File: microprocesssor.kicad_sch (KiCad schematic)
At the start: 8 parts, among them U1 MC68B09, U11 74LS138, U2 MC68B40, U4 27128, U5 HM62256BLP, U6 74LS139, X1 CXO_DIP8

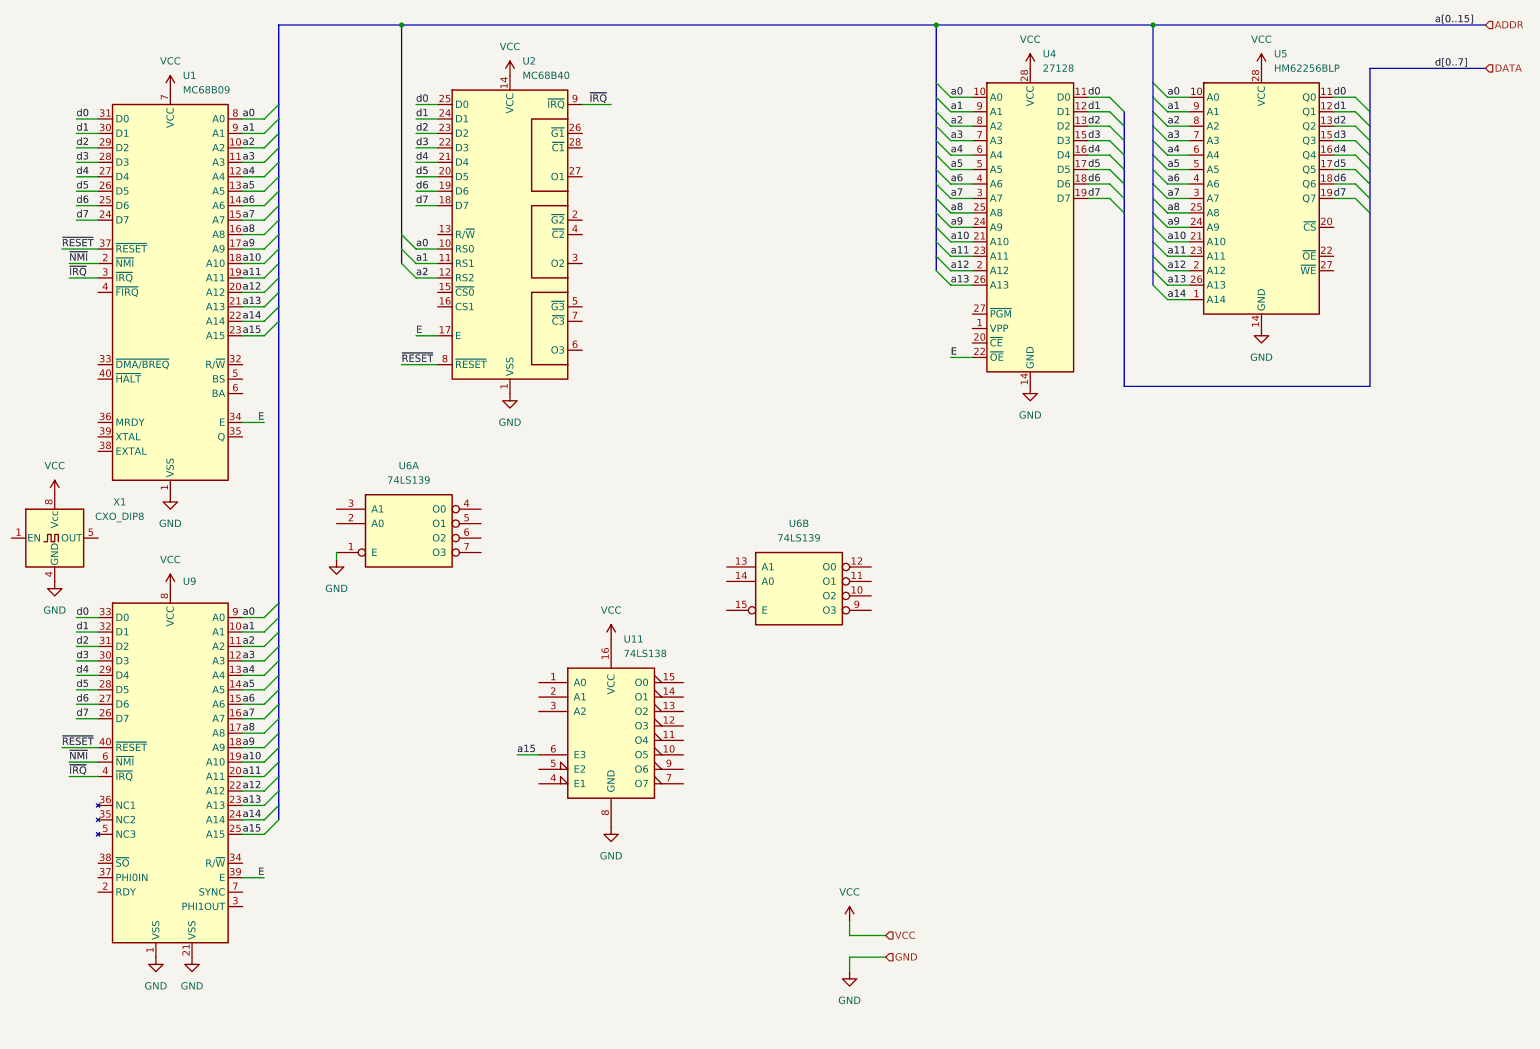
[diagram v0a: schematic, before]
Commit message: Update schematic.
Pull-up resistors for 6809 signals. 74LS251 mux for 8 input pins. MIDI optoisolator. Wire up 74LS139 for RD and WR. Still many unconnected pins. TODO: connect sheets with control bus.
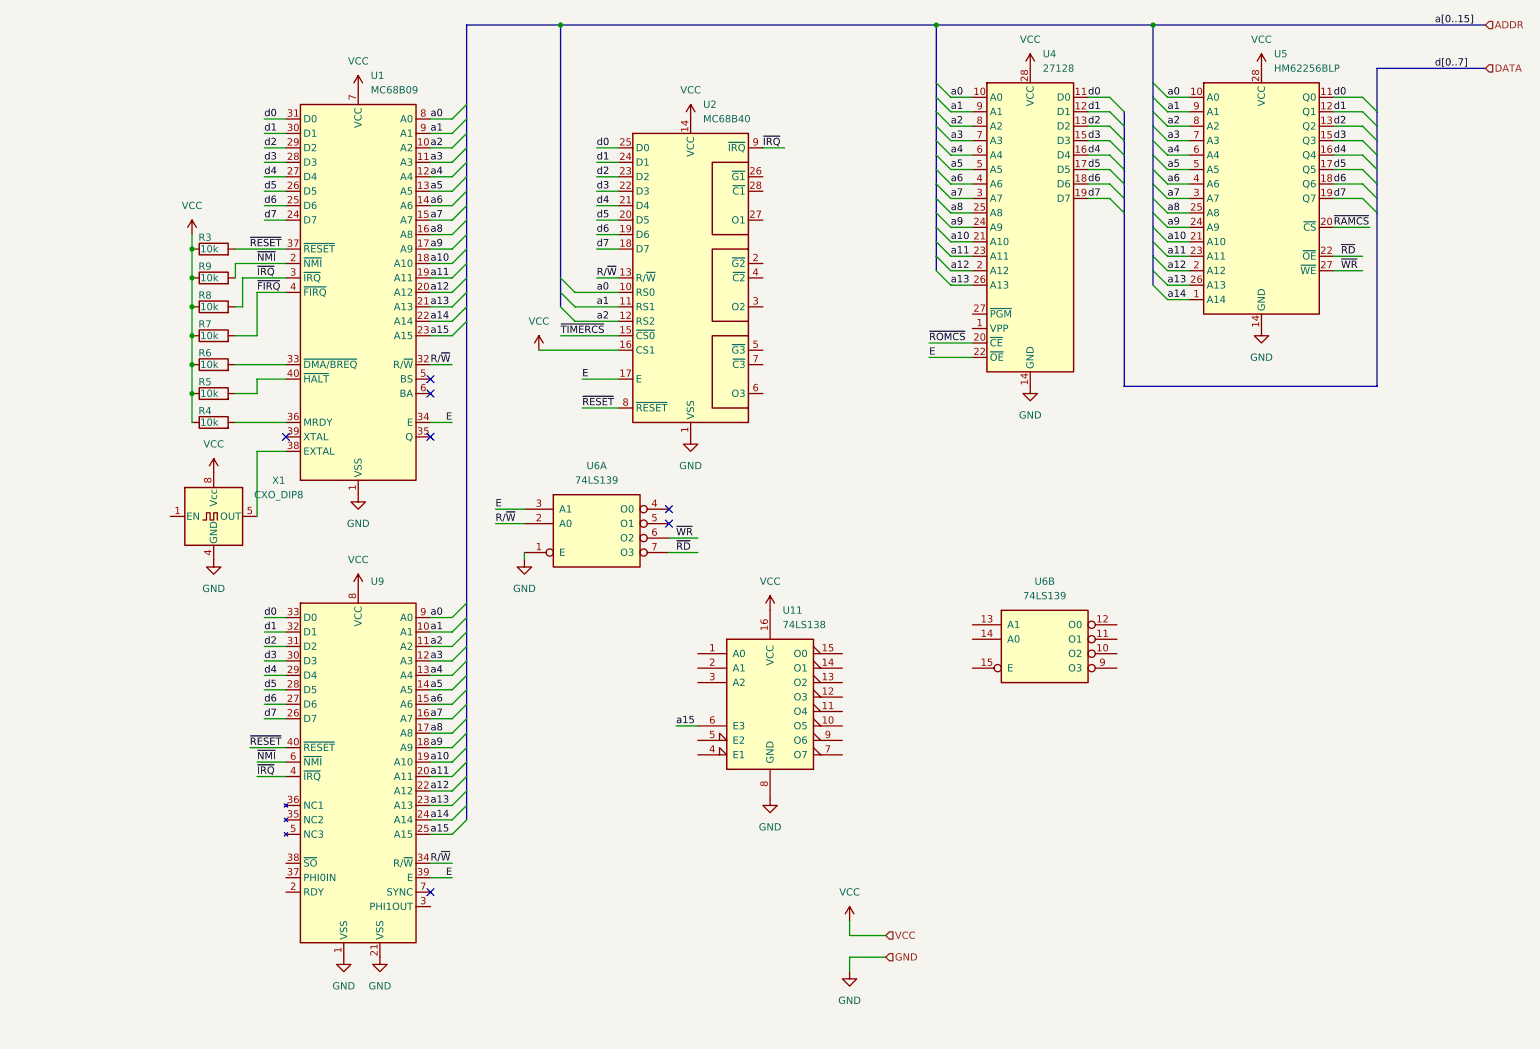
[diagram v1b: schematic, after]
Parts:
- added R3, R4, R5, R6, R7, R8, R9: 10k, symbol Device:R
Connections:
- net E: now also U6.3 (A1)
- net VCC: now also U2.16 (CS1), R3.1, R4.1, R5.1, R6.1, R7.1, R8.1, R9.1
- net ~{IRQ}: now also R8.2
- net ~{NMI}: now also R9.2
- net ~{RESET}: now also R3.2
- net R/~{W}: now reaches U6.2 (A0)
- net R/~{W}: now also U1.32 (R/~{W}), U2.13 (R/~{W}), U9.34 (R/~{W})
- net ~{WR}: now reaches U6.6 (O2)
- net ~{WR}: now also U5.27 (~{WE})
- net ~{RD}: now reaches U6.7 (O3)
- net ~{RD}: now also U5.22 (~{OE})
- net ~{ROMCS}: now reaches U4.20 (~{CE})
- net ~{TIMERCS}: now reaches U2.15 (~{CS0})
- net ~{RAMCS}: now reaches U5.20 (~{CS})
- net at U1.33 (~{DMA/BREQ}): now also R6.2
- net at U1.36 (MRDY): now also R4.2
- net at U1.38 (EXTAL): now also X1.5 (OUT)
- net ~{FIRQ}: now reaches U1.4 (~{FIRQ})
- net ~{FIRQ}: now also R7.2
- net at U1.40 (~{HALT}): now also R5.2
- no-connect marks 0 -> 7
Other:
- moved on the sheet: U1, U11, U2, U6A, U6B, U9, X1

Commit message: Add INTS bus, address decoder, and I2C chip.
INTS bus carries RESET, NMI, FIRQ, and IRQ. Only RESET and IRQ used so far. Philips PCF8584 I2C interface chp added. Address decoder added based on 74LS139 and two 74LS138s. TODO: add CTRL bus with E, R/W, RD, and WR.
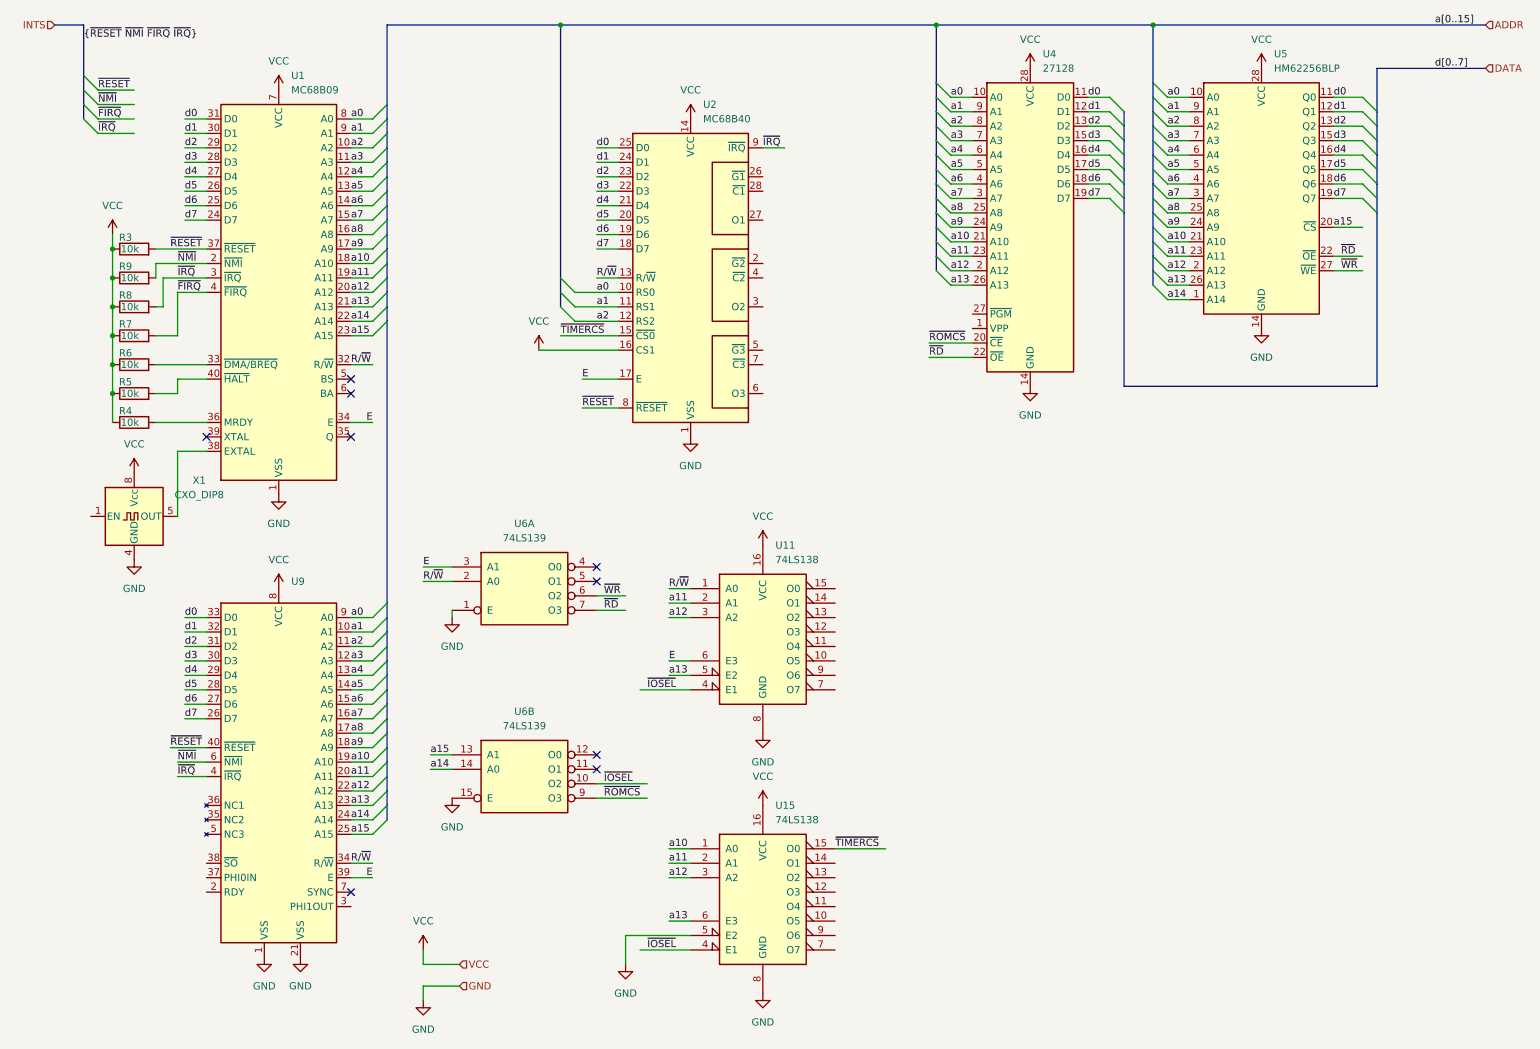
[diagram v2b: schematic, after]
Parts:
- added U15: 74LS138, Package_DIP:DIP-16_W7.62mm, symbol 74xx:74LS138
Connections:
- net ~{RAMCS} is gone; now on net a15: U5.20 (~{CS})
- net E: now also U11.6 (E3); no longer U4.22 (~{OE})
- net GND: now also U6.15 (E), U15.5 (E2), U15.8 (GND)
- net R/~{W}: now also U11.1 (A0)
- net VCC: now also U15.16 (VCC)
- net a10: now also U15.1 (A0)
- net a11: now also U11.2 (A1), U15.2 (A1)
- net a12: now also U11.3 (A2), U15.3 (A2)
- net a13: now also U11.5 (E2), U15.6 (E3)
- net a14: now also U6.14 (A0)
- net a15: now also U6.13 (A1); no longer U11.6 (E3)
- net ~{RD}: now also U4.22 (~{OE})
- net ~{ROMCS}: now also U6.9 (O3)
- net ~{TIMERCS}: now also U15.15 (O0)
- net ~{IOSEL}: now reaches U11.4 (E1)
- net ~{IOSEL}: now also U6.10 (O2), U15.4 (E1)
- no-connect marks 7 -> 9
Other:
- moved on the sheet: R3, R4, R5, R6, R7, R8, R9, U1, U11, U6A, U6B, U9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

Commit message: Add control bus.
R/W, E, RD, WR signals from microprocessor to GPIO.
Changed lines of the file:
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@@
 	)
 	(bus_entry
+		(at 270.51 46.99)
+		(size 2.54 -2.54)
+		(stroke
+			(width 0)
+			(type default)
+		)
+	)
+	(bus_entry
 		(at 80.01 64.77)
 		(size 2.54 -2.54)
@@
 	)
 	(bus_entry
+		(at 270.51 39.37)
+		(size 2.54 -2.54)
+		(stroke
+			(width 0)
+			(type default)
+		)
+	)
+	(bus_entry
 		(at 181.61 53.34)
 		(size -2.54 -2.54)
@@
 	)
 	(bus_entry
+		(at 270.51 44.45)
+		(size 2.54 -2.54)
+		(stroke
+			(width 0)
+			(type default)
+		)
+	)
+	(bus_entry
 		(at 181.61 63.5)
 		(size -2.54 -2.54)
@@
 	)
 	(bus_entry
+		(at 270.51 41.91)
+		(size 2.54 -2.54)
+		(stroke
+			(width 0)
+			(type default)
+		)
+	)
+	(bus_entry
 		(at 31.75 31.75)
 		(size -2.54 -2.54)
@@
 	(bus
 		(pts
+			(xy 273.05 36.83) (xy 273.05 39.37)
+		)
+		(stroke
+			(width 0)
+			(type default)
+		)
+	)
+	(bus
+		(pts
 			(xy 113.03 62.23) (xy 113.03 64.77)
 		)
@@
 	(bus
 		(pts
+			(xy 273.05 33.02) (xy 273.05 36.83)
+		)
+		(stroke
+			(width 0)
+			(type default)
+		)
+	)
+	(bus
+		(pts
 			(xy 82.55 64.77) (xy 82.55 67.31)
 		)
@@
 	(wire
 		(pts
+			(xy 264.16 41.91) (xy 270.51 41.91)
+		)
+		(stroke
+			(width 0)
+			(type default)
+		)
+	)
+	(wire
+		(pts
 			(xy 205.74 33.02) (xy 209.55 33.02)
 		)
@@
 	(bus
 		(pts
+			(xy 273.05 41.91) (xy 273.05 44.45)
+		)
+		(stroke
+			(width 0)
+			(type default)
+		)
+	)
+	(bus
+		(pts
 			(xy 82.55 139.7) (xy 82.55 142.24)
 		)
@@
 		)
 	)
+	(bus
+		(pts
+			(xy 273.05 39.37) (xy 273.05 41.91)
+		)
+		(stroke
+			(width 0)
+			(type default)
+		)
+	)
 	(wire
 		(pts
@@
 	(wire
 		(pts
+			(xy 270.51 39.37) (xy 264.16 39.37)
+		)
+		(stroke
+			(width 0)
+			(type default)
+		)
+	)
+	(wire
+		(pts
 			(xy 43.18 62.23) (xy 50.8 62.23)
 		)
@@
 	(wire
 		(pts
+			(xy 270.51 44.45) (xy 264.16 44.45)
+		)
+		(stroke
+			(width 0)
+			(type default)
+		)
+	)
+	(wire
+		(pts
 			(xy 76.2 157.48) (xy 80.01 157.48)
 		)
@@
 	(wire
 		(pts
+			(xy 270.51 46.99) (xy 264.16 46.99)
+		)
+		(stroke
+			(width 0)
+			(type default)
+		)
+	)
+	(wire
+		(pts
 			(xy 181.61 48.26) (xy 185.42 48.26)
 		)
@@
 		)
 	)
+	(bus
+		(pts
+			(xy 275.59 33.02) (xy 273.05 33.02)
+		)
+		(stroke
+			(width 0)
+			(type default)
+		)
+	)
 	(wire
 		(pts
@@
 		)
 	)
+	(label "R{slash}~{W}"
+		(at 270.51 39.37 180)
+		(fields_autoplaced yes)
+		(effects
+			(font
+				(size 1.27 1.27)
+			)
+			(justify right bottom)
+		)
+	)
 	(label "d1"
 		(at 46.99 36.83 0)
@@
 		)
 	)
+	(label "~{WR}"
+		(at 270.51 46.99 180)
+		(fields_autoplaced yes)
+		(effects
+			(font
+				(size 1.27 1.27)
+			)
+			(justify right bottom)
+		)
+	)
 	(label "d2"
 		(at 205.74 35.56 0)
@@
 		)
 	)
+	(label "~{RD}"
+		(at 270.51 44.45 180)
+		(fields_autoplaced yes)
+		(effects
+			(font
+				(size 1.27 1.27)
+			)
+			(justify right bottom)
+		)
+	)
 	(label "a0"
 		(at 181.61 30.48 0)
@@
 		)
 	)
+	(label "{R{slash}~{W} E ~{RD} ~{WR}}"
+		(at 273.05 35.56 180)
+		(fields_autoplaced yes)
+		(effects
+			(font
+				(size 1.27 1.27)
+			)
+			(justify right bottom)
+		)
+	)
 	(label "~{ROMCS}"
 		(at 120.65 153.67 0)
@@
 		)
 	)
+	(label "E"
+		(at 269.24 41.91 0)
+		(fields_autoplaced yes)
+		(effects
+			(font
+				(size 1.27 1.27)
+			)
+			(justify left bottom)
+		)
+	)
 	(label "R{slash}~{W}"
 		(at 76.2 165.1 0)
@@
 		(fields_autoplaced yes)
 		(effects
+			(font
+				(size 1.27 1.27)
+			)
+			(justify left)
+		)
+	)
+	(hierarchical_label "CTRL"
+		(shape input)
+		(at 275.59 33.02 0)
+		(fields_autoplaced yes)
+		(effects

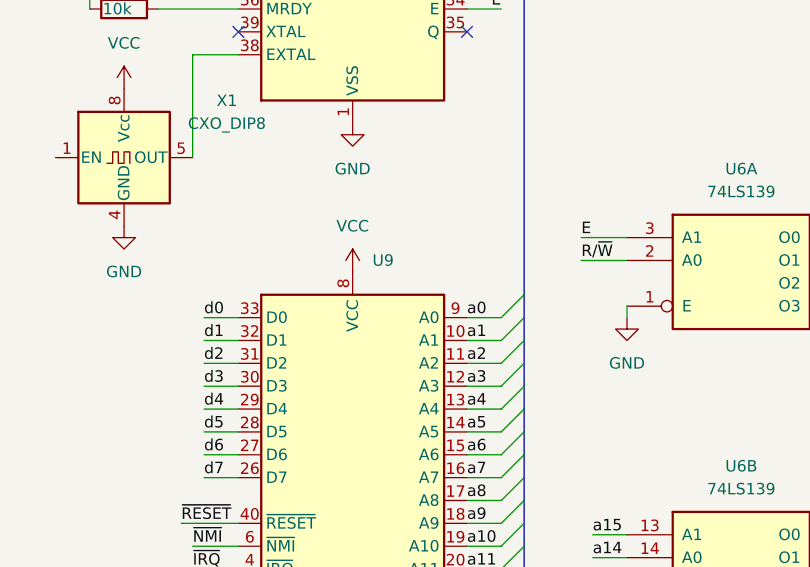
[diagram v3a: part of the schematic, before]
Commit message: Replace 6551 with R65C52 (dual ACIA).
New symbol for R65C52 in library. Two async serial ports in one 40-pin package. But it has no 'E' input. Also remove two misconnected WR and RD pins.
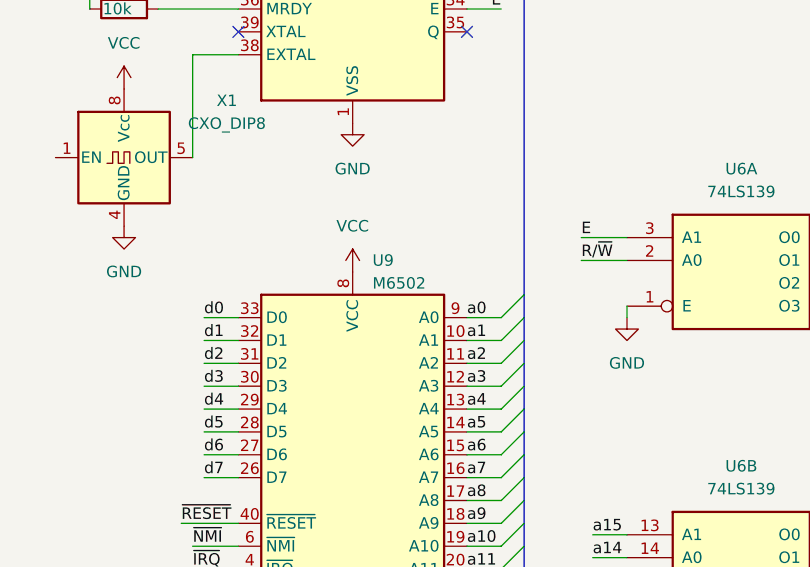
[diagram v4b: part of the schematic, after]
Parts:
- U9: value ~ -> M6502
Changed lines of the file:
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@@
 			)
 		)
-		(property "Value" "~"
+		(property "Value" "M6502"
 			(at 65.6941 118.11 0)
 			(effects
